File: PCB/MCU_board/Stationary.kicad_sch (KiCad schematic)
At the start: 13 parts, among them IC1 NEO-F10N-00B, IC6 4259-63, IC8 MAX98357AETE+T, J2 Speaker, J4 FXP612 (u.FL) 2, J5 FXP612 (u.FL) 1, Q3 Si2323DDS-T1-GE3, Q4 BSS138

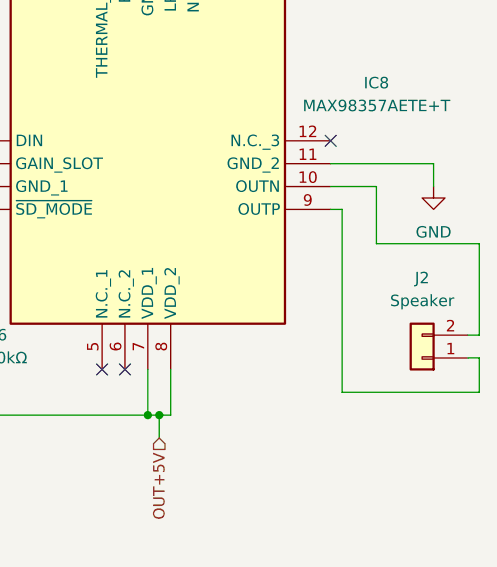
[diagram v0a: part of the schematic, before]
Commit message: routing and holes added
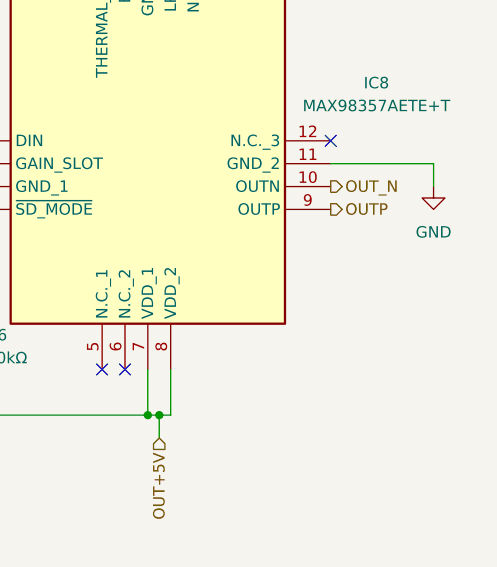
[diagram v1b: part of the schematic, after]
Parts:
- removed J2: Speaker, Connector_JST:JST_PH_B2B-PH-K_1x02_P2.00mm_Vertical, symbol Connector_Generic:Conn_01x02
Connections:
- net OUT_N: now reaches IC8.10 (OUTN)
- net OUTP: now reaches IC8.9 (OUTP)
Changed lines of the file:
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@@
+	)
+	(junction
+		(at 15.24 62.23)
+		(diameter 0)
+		(color 0 0 0 0)
 	)
 	(junction
@@
 		(color 0 0 0 0)
 	)
-	(junction
-		(at 15.24 62.23)
-		(diameter 0)
-		(color 0 0 0 0)
-	)
 	(no_connect
 		(at 39.37 36.83)
@@
 	(wire
 		(pts
-			(xy 275.59 87.63) (xy 275.59 91.44)
-		)
-		(stroke
-			(width 0)
-			(type default)
-		)
-	)
-	(wire
-		(pts
 			(xy 110.49 59.69) (xy 110.49 64.77)
 		)
@@
 	(wire
 		(pts
-			(xy 259.08 68.58) (xy 264.16 68.58)
-		)
-		(stroke
-			(width 0)
-			(type default)
-		)
-	)
-	(wire
-		(pts
 			(xy 54.61 114.3) (xy 54.61 106.68)
 		)
@@
 	(wire
 		(pts
-			(xy 275.59 91.44) (xy 260.35 91.44)
-		)
-		(stroke
-			(width 0)
-			(type default)
-		)
-	)
-	(wire
-		(pts
 			(xy 15.24 62.23) (xy 15.24 64.77)
 		)
@@
 	(wire
 		(pts
-			(xy 275.59 85.09) (xy 275.59 74.93)
-		)
-		(stroke
-			(width 0)
-			(type default)
-		)
-	)
-	(wire
-		(pts
 			(xy 27.94 101.6) (xy 31.75 101.6)
 		)
@@
 	(wire
 		(pts
-			(xy 264.16 74.93) (xy 264.16 68.58)
-		)
-		(stroke
-			(width 0)
-			(type default)
-		)
-	)
-	(wire
-		(pts
 			(xy 58.42 173.99) (xy 62.23 173.99)
 		)
@@
 	(wire
 		(pts
-			(xy 275.59 74.93) (xy 264.16 74.93)
-		)
-		(stroke
-			(width 0)
-			(type default)
-		)
-	)
-	(wire
-		(pts
 			(xy 241.3 88.9) (xy 241.3 93.98)
 		)
@@
 	(wire
 		(pts
-			(xy 260.35 91.44) (xy 260.35 71.12)
-		)
-		(stroke
-			(width 0)
-			(type default)
-		)
-	)
-	(wire
-		(pts
 			(xy 129.54 87.63) (xy 129.54 77.47)
 		)
@@
 	(wire
 		(pts
-			(xy 274.32 85.09) (xy 275.59 85.09)
-		)
-		(stroke
-			(width 0)
-			(type default)
-		)
-	)
-	(wire
-		(pts
 			(xy 200.66 97.79) (xy 200.66 100.33)
 		)
@@
 		(pts
 			(xy 82.55 57.15) (xy 92.71 57.15)
-		)
-		(stroke
-			(width 0)
-			(type default)
-		)
-	)
-	(wire
-		(pts
-			(xy 274.32 87.63) (xy 275.59 87.63)
-		)
-		(stroke
-			(width 0)
-			(type default)
-		)
-	)
-	(wire
-		(pts
-			(xy 260.35 71.12) (xy 259.08 71.12)
 		)
 		(stroke
@@
 		)
 	)
+	(hierarchical_label "OUT_N"
+		(shape output)
+		(at 259.08 68.58 0)
+		(effects
+			(font
+				(size 1.27 1.27)
+			)
+			(justify left)
+		)
+	)
 	(hierarchical_label "GPS_POWER"
 		(shape input)
@@
 		(shape output)
 		(at 86.36 54.61 0)
+		(effects
+			(font
+				(size 1.27 1.27)
+			)
+			(justify left)
+		)
+	)
+	(hierarchical_label "OUTP"
+		(shape output)
+		(at 259.08 71.12 0)
 		(effects
 			(font
@@
 					(unit 1)
 				)
-			)
-		)
-	)
-	(symbol
-		(lib_id "Connector_Generic:Conn_01x02")
-		(at 269.24 87.63 180)
-		(unit 1)
-		(body_style 1)
-		(exclude_from_sim no)
-		(in_bom yes)
-		(on_board yes)
-		(in_pos_files yes)
-		(dnp no)
-		(fields_autoplaced yes)
-		(property "Reference" "J2"
-			(at 269.24 78.74 0)
-			(show_name no)
-			(do_not_autoplace no)
-			(effects
-				(font
-					(size 1.27 1.27)
-				)
-			)
-		)
-		(property "Value" "Speaker"
-			(at 269.24 81.28 0)
-			(show_name no)
-			(do_not_autoplace no)
-			(effects
-				(font
-					(size 1.27 1.27)
-				)
-			)
-		)
-		(property "Footprint" "Connector_JST:JST_PH_B2B-PH-K_1x02_P2.00mm_Vertical"
-			(at 269.24 87.63 0)
-			(hide yes)
-			(show_name no)
-			(do_not_autoplace no)
-			(effects
-				(font
-					(size 1.27 1.27)
-				)
-			)
-		)
-		(property "Datasheet" ""
-			(at 269.24 87.63 0)
-			(hide yes)
-			(show_name no)
-			(do_not_autoplace no)
-			(effects
-				(font
-					(size 1.27 1.27)
-				)
-			)
-		)
-		(property "Description" "Generic connector, single row, 01x02, script generated (kicad-library-utils/schlib/autogen/connector/)"
-			(at 269.24 87.63 0)
-			(hide yes)
-			(show_name no)
-			(do_not_autoplace no)
-			(effects
-				(font
-					(size 1.27 1.27)
-				)
-			)
-		)
-		(pin "2"
-		)
-		(pin "1"
-		)
-		(instances
-			(project "MCU_board"
-				(path "/498aac81-136e-41bd-a3ff-29bc0732936d/cfe949ab-0502-475b-aed9-50a88bd6f7c8"
-					(reference "J2")
-					(unit 1)
-				)

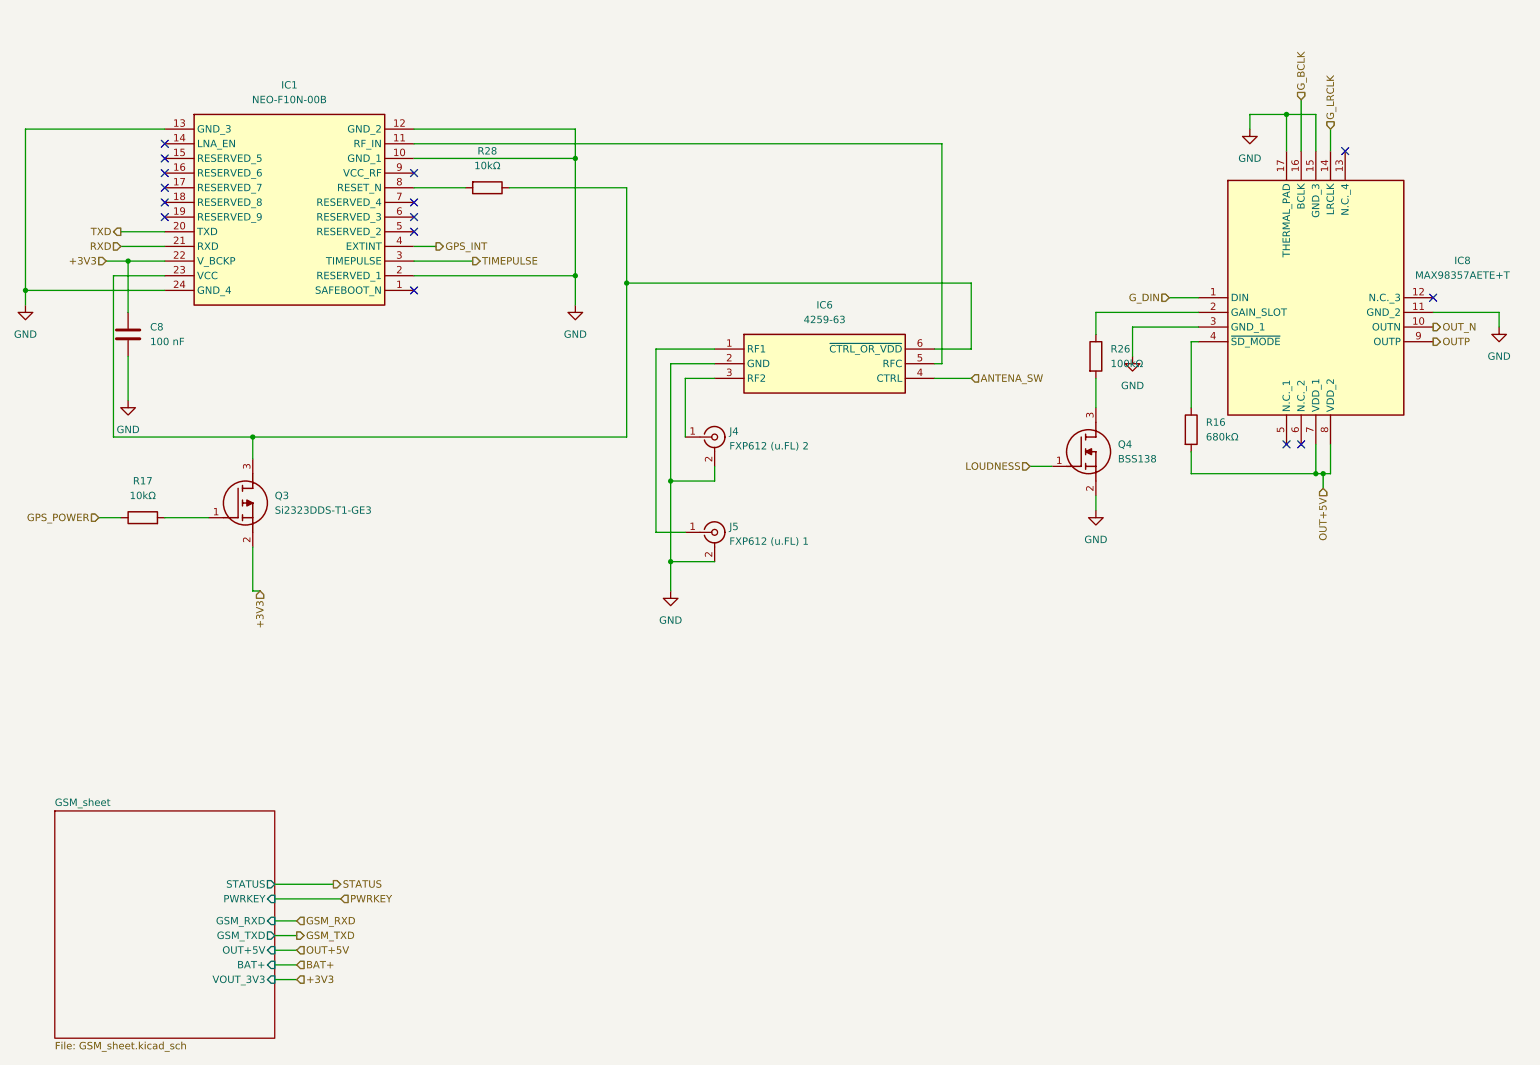
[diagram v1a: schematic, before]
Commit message: verifying schematic and 3V8 power for gsm
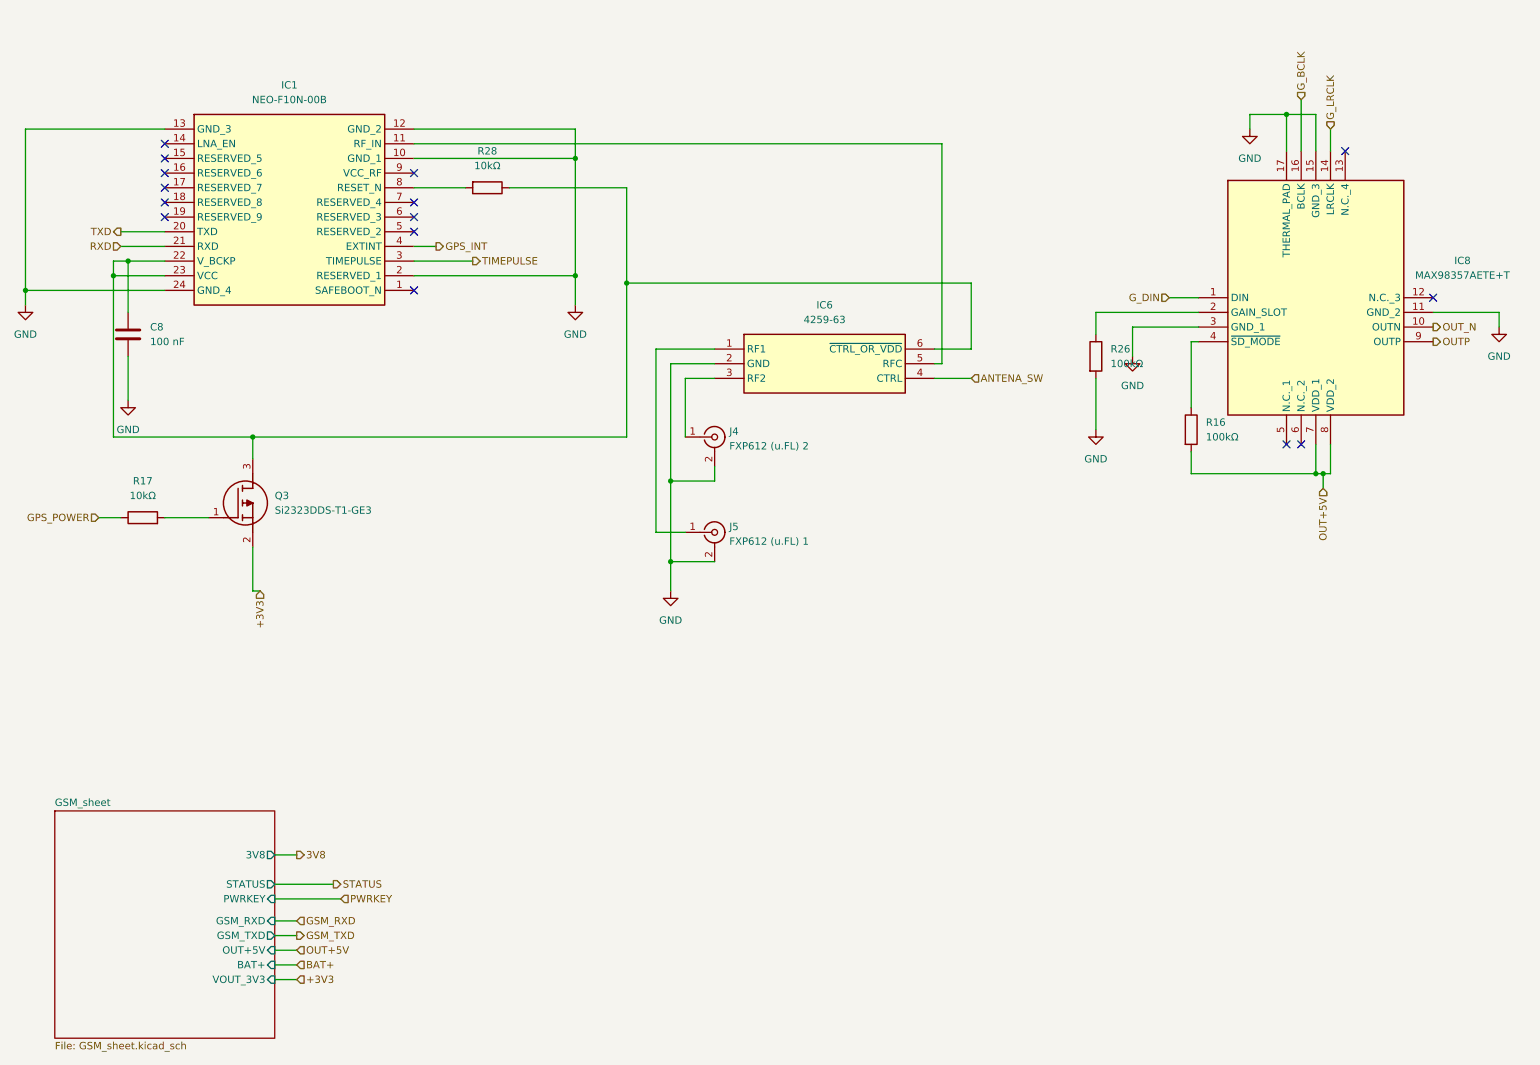
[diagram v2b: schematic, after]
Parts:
- removed Q4: BSS138, BSS138:SOT95P240X120-3N, symbol BSS138:BSS138
- R16: value 680kΩ -> 100kΩ
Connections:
- net +3V3: no longer C8.1, IC1.22 (V_BCKP)
- net GND: now also R26.2
- net at IC1.23 (VCC), IC6.6 (~{CTRL_OR_VDD}), Q3.3 (D)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: now also C8.1, IC1.22 (V_BCKP)
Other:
- sheet GSM_sheet ports: added 3V8; removed none
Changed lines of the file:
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@@
 	)
 	(junction
-		(at 33.02 57.15)
+		(at 238.76 93.98)
 		(diameter 0)
 		(color 0 0 0 0)
 	)
 	(junction
-		(at 238.76 93.98)
+		(at 240.03 93.98)
 		(diameter 0)
 		(color 0 0 0 0)
 	)
 	(junction
-		(at 240.03 93.98)
+		(at 127 95.25)
 		(diameter 0)
 		(color 0 0 0 0)
 	)
 	(junction
-		(at 127 95.25)
+		(at 33.02 57.15)
 		(diameter 0)
 		(color 0 0 0 0)
@@
 	)
 	(junction
+		(at 30.48 59.69)
+		(diameter 0)
+		(color 0 0 0 0)
+	)
+	(junction
 		(at 119.38 60.96)
 		(diameter 0)
@@
 	(wire
 		(pts
-			(xy 200.66 77.47) (xy 200.66 82.55)
-		)
-		(stroke
-			(width 0)
-			(type default)
-		)
-	)
-	(wire
-		(pts
-			(xy 29.21 57.15) (xy 33.02 57.15)
+			(xy 30.48 57.15) (xy 30.48 59.69)
 		)
 		(stroke
@@
 	(wire
 		(pts
+			(xy 200.66 77.47) (xy 200.66 86.36)
+		)
+		(stroke
+			(width 0)
+			(type default)
+		)
+	)
+	(wire
+		(pts
 			(xy 33.02 73.66) (xy 33.02 81.28)
 		)
@@
 	(wire
 		(pts
-			(xy 189.23 92.71) (xy 193.04 92.71)
+			(xy 58.42 173.99) (xy 62.23 173.99)
 		)
 		(stroke
@@
 	(wire
 		(pts
-			(xy 58.42 173.99) (xy 62.23 173.99)
+			(xy 33.02 57.15) (xy 30.48 57.15)
 		)
 		(stroke
@@
 	(wire
 		(pts
-			(xy 39.37 101.6) (xy 46.99 101.6)
+			(xy 58.42 160.02) (xy 62.23 160.02)
 		)
 		(stroke
@@
 	(wire
 		(pts
-			(xy 200.66 97.79) (xy 200.66 100.33)
+			(xy 39.37 101.6) (xy 46.99 101.6)
 		)
 		(stroke
@@
 		)
 	)
-	(hierarchical_label "LOUDNESS"
-		(shape input)
-		(at 189.23 92.71 180)
-		(effects
-			(font
-				(size 1.27 1.27)
-			)
-			(justify right)
-		)
-	)
 	(hierarchical_label "G_LRCLK"
 		(shape input)
@@
 		)
 	)
-	(hierarchical_label "PWRKEY"
-		(shape input)
-		(at 69.85 167.64 0)
+	(hierarchical_label "3V8"
+		(shape output)
+		(at 62.23 160.02 0)
 		(effects
 			(font
@@
 		)
 	)
-	(hierarchical_label "+3V3"
+	(hierarchical_label "PWRKEY"
 		(shape input)
-		(at 62.23 181.61 0)
+		(at 69.85 167.64 0)
 		(effects
 			(font
@@
 	(hierarchical_label "+3V3"
 		(shape input)
-		(at 29.21 57.15 180)
+		(at 62.23 181.61 0)
 		(effects
 			(font
 				(size 1.27 1.27)
 			)
-			(justify right)
+			(justify left)
 		)
 	)
@@
 			)
 		)
-		(property "Value" "680kΩ"
+		(property "Value" "100kΩ"
 			(at 219.71 87.6299 0)
 			(show_name no)
@@
 	)
 	(symbol
-		(lib_id "power:GND")
-		(at 200.66 100.33 0)
-		(unit 1)
-		(body_style 1)
-		(exclude_from_sim no)
-		(in_bom yes)
-		(on_board yes)
-		(in_pos_files yes)
-		(dnp no)
-		(fields_autoplaced yes)
-		(property "Reference" "#PWR036"
-			(at 200.66 106.68 0)
-			(hide yes)
-			(show_name no)
-			(do_not_autoplace no)
-			(effects
-				(font
-					(size 1.27 1.27)
-				)
-			)
-		)
-		(property "Value" "GND"
-			(at 200.66 105.41 0)
-			(show_name no)
-			(do_not_autoplace no)
-			(effects
-				(font
-					(size 1.27 1.27)
-				)
-			)
-		)
-		(property "Footprint" ""
-			(at 200.66 100.33 0)
-			(hide yes)
-			(show_name no)
-			(do_not_autoplace no)
-			(effects
-				(font
-					(size 1.27 1.27)
-				)
-			)
-		)
-		(property "Datasheet" ""
-			(at 200.66 100.33 0)
-			(hide yes)
-			(show_name no)
-			(do_not_autoplace no)
-			(effects
-				(font
-					(size 1.27 1.27)
-				)
-			)
-		)
-		(property "Description" "Power symbol creates a global label with name \"GND\" , ground"
-			(at 200.66 100.33 0)
-			(hide yes)
-			(show_name no)
-			(do_not_autoplace no)
-			(effects
-				(font
-					(size 1.27 1.27)
-				)
-			)
-		)
-		(pin "1"
-		)
-		(instances
-			(project "MCU_board"
-				(path "/498aac81-136e-41bd-a3ff-29bc0732936d/cfe949ab-0502-475b-aed9-50a88bd6f7c8"
-					(reference "#PWR036")
-					(unit 1)
-				)
-			)
-		)
-	)
-	(symbol
 		(lib_id "MAX98357AETE+T:MAX98357AETE+T")
 		(at 218.44 63.5 0)
@@
 	(symbol
 		(lib_id "power:GND")
+		(at 200.66 86.36 0)
+		(unit 1)
+		(body_style 1)
+		(exclude_from_sim no)
+		(in_bom yes)
+		(on_board yes)
+		(in_pos_files yes)
+		(dnp no)
+		(fields_autoplaced yes)
+		(property "Reference" "#PWR04"
+			(at 200.66 92.71 0)
+			(hide yes)
+			(show_name no)
+			(do_not_autoplace no)
+			(effects
+				(font
+					(size 1.27 1.27)
+				)
+			)
+		)
+		(property "Value" "GND"
+			(at 200.66 91.44 0)
+			(show_name no)
+			(do_not_autoplace no)
+			(effects
+				(font
+					(size 1.27 1.27)
+				)
+			)
+		)
+		(property "Footprint" ""
+			(at 200.66 86.36 0)
+			(hide yes)
+			(show_name no)
+			(do_not_autoplace no)
+			(effects
+				(font
+					(size 1.27 1.27)
+				)
+			)
+		)
+		(property "Datasheet" ""
+			(at 200.66 86.36 0)
+			(hide yes)
+			(show_name no)
+			(do_not_autoplace no)
+			(effects
+				(font
+					(size 1.27 1.27)
+				)
+			)
+		)
+		(property "Description" "Power symbol creates a global label with name \"GND\" , ground"
+			(at 200.66 86.36 0)
+			(hide yes)
+			(show_name no)
+			(do_not_autoplace no)
+			(effects
+				(font
+					(size 1.27 1.27)
+				)
+			)
+		)
+		(pin "1"
+		)
+		(instances
+			(project "MCU_board"
+				(path "/498aac81-136e-41bd-a3ff-29bc0732936d/cfe949ab-0502-475b-aed9-50a88bd6f7c8"
+					(reference "#PWR04")
+					(unit 1)
+				)
+			)
+		)
+	)
+	(symbol
+		(lib_id "power:GND")
 		(at 15.24 64.77 0)
 		(unit 1)
@@
 	)
 	(symbol
-		(lib_id "BSS138:BSS138")
-		(at 193.04 92.71 0)
-		(unit 1)
-		(body_style 1)
-		(exclude_from_sim no)
-		(in_bom yes)
-		(on_board yes)
-		(in_pos_files yes)
-		(dnp no)
-		(fields_autoplaced yes)
-		(property "Reference" "Q4"
-			(at 204.47 88.8999 0)
-			(show_name no)
-			(do_not_autoplace no)
-			(effects
-				(font
-					(size 1.27 1.27)
-				)
-				(justify left)
-			)
-		)
-		(property "Value" "BSS138"
-			(at 204.47 91.4399 0)
-			(show_name no)
-			(do_not_autoplace no)
-			(effects
-				(font
-					(size 1.27 1.27)
-				)
-				(justify left)
-			)
-		)
-		(property "Footprint" "BSS138:SOT95P240X120-3N"
-			(at 204.47 191.44 0)
-			(hide yes)
-			(show_name no)
-			(do_not_autoplace no)
-			(effects
-				(font
-					(size 1.27 1.27)
-				)
-				(justify left top)
-			)
-		)
-		(property "Datasheet" "https://www.onsemi.com/pub/Collateral/BSS138-D.PDF"
-			(at 204.47 291.44 0)
-			(hide yes)
-			(show_name no)
-			(do_not_autoplace no)
-			(effects
-				(font
-					(size 1.27 1.27)
-				)
-				(justify left top)
-			)
-		)
-		(property "Description" "Compact industry standard SOT-23 surface mount package.; 0.22 A, 50 V. RDS(ON) = 3.5  @ VGS = 10 V. RDS(ON) = 6.0  @ VGS = 4.5 V; Rugged and Reliable.; High density cell design for extremely low RDS(ON)."
-			(at 193.04 92.71 0)
-			(hide yes)
-			(show_name no)
-			(do_not_autoplace no)
-			(effects
-				(font
-					(size 1.27 1.27)
-				)
-			)
-		)
-		(property "Height" "1.2"
-			(at 204.47 491.44 0)
-			(hide yes)
-			(show_name no)
-			(do_not_autoplace no)
-			(effects
-				(font
-					(size 1.27 1.27)
-				)
-				(justify left top)
-			)
-		)
-		(property "Mouser Part Number" "512-BSS138"
-			(at 204.47 591.44 0)
-			(hide yes)
-			(show_name no)
-			(do_not_autoplace no)
-			(effects
-				(font
-					(size 1.27 1.27)
-				)
-				(justify left top)
-			)
-		)
-		(property "Mouser Price/Stock" "https://www.mouser.co.uk/ProductDetail/onsemi-Fairchild/BSS138?qs=HK%252BeIG1iaahCeqBvjB4arg%3D%3D"
-			(at 204.47 691.44 0)
-			(hide yes)
-			(show_name no)
-			(do_not_autoplace no)
-			(effects
-				(font
-					(size 1.27 1.27)
-				)
-				(justify left top)
-			)
-		)
-		(property "Manufacturer_Name" "onsemi"
-			(at 204.47 791.44 0)
-			(hide yes)
-			(show_name no)
-			(do_not_autoplace no)
-			(effects
-				(font
-					(size 1.27 1.27)
-				)
-				(justify left top)
-			)
-		)
-		(property "Manufacturer_Part_Number" "BSS138"
-			(at 204.47 891.44 0)
-			(hide yes)
-			(show_name no)
-			(do_not_autoplace no)
-			(effects
-				(font
-					(size 1.27 1.27)
-				)
-				(justify left top)
-			)
-		)
-		(pin "3"
-		)
-		(pin "2"
-		)
-		(pin "1"
-		)
-		(instances
-			(project "MCU_board"
-				(path "/498aac81-136e-41bd-a3ff-29bc0732936d/cfe949ab-0502-475b-aed9-50a88bd6f7c8"
-					(reference "Q4")
-					(unit 1)
-				)
-			)
-		)
-	)
-	(symbol
 		(lib_id "Device:R")
 		(at 200.66 73.66 0)
@@
 			(effects
 				(font
+					(size 1.27 1.27)
+				)
+				(justify right)
+			)
+		)
+		(pin "3V8" output
+			(at 58.42 160.02 0)
+			(effects
+				(font

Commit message: ECR passed
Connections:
- net OUT+5V: no longer R16.2
- new net LOUDNESS: R16.2
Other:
- sheet GSM_sheet ports: added none; removed BAT+, OUT+5V
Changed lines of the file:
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@@
-	)
-	(junction
-		(at 238.76 93.98)
-		(diameter 0)
-		(color 0 0 0 0)
 	)
 	(junction
@@
 	(wire
 		(pts
-			(xy 58.42 179.07) (xy 62.23 179.07)
-		)
-		(stroke
-			(width 0)
-			(type default)
-		)
-	)
-	(wire
-		(pts
 			(xy 127 95.25) (xy 134.62 95.25)
 		)
@@
 	(wire
 		(pts
-			(xy 58.42 176.53) (xy 62.23 176.53)
-		)
-		(stroke
-			(width 0)
-			(type default)
-		)
-	)
-	(wire
-		(pts
-			(xy 217.17 93.98) (xy 238.76 93.98)
-		)
-		(stroke
-			(width 0)
-			(type default)
-		)
-	)
-	(wire
-		(pts
 			(xy 129.54 77.47) (xy 134.62 77.47)
 		)
@@
 		(pts
 			(xy 82.55 39.37) (xy 110.49 39.37)
+		)
+		(stroke
+			(width 0)
+			(type default)
+		)
+	)
+	(wire
+		(pts
+			(xy 217.17 93.98) (xy 219.71 93.98)
 		)
 		(stroke
@@
 		)
 	)
+	(hierarchical_label "LOUDNESS"
+		(shape input)
+		(at 219.71 93.98 0)
+		(effects
+			(font
+				(size 1.27 1.27)
+			)
+			(justify left)
+		)
+	)
 	(hierarchical_label "G_DIN"
 		(shape input)
@@
 		)
 	)
-	(hierarchical_label "OUT+5V"
-		(shape input)
-		(at 62.23 176.53 0)
-		(effects
-			(font
-				(size 1.27 1.27)
-			)
-			(justify left)
-		)
-	)
 	(hierarchical_label "ANTENA_SW"
 		(shape input)
@@
 		(shape input)
 		(at 241.3 34.29 90)
-		(effects
-			(font
-				(size 1.27 1.27)
-			)
-			(justify left)
-		)
-	)
-	(hierarchical_label "BAT+"
-		(shape input)
-		(at 62.23 179.07 0)
 		(effects
 			(font
@@
 			)
 		)
-		(pin "BAT+" input
-			(at 58.42 179.07 0)
-			(effects
-				(font
-					(size 1.27 1.27)
-				)
-				(justify right)
-			)
-		)
 		(pin "GSM_RXD" input
 			(at 58.42 171.45 0)
@@
 			(effects
 				(font
-					(size 1.27 1.27)
-				)
-				(justify right)
-			)
-		)
-		(pin "OUT+5V" input
-			(at 58.42 176.53 0)
-			(effects
-				(font
